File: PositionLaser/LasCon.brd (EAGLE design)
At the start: 44.4 x 28 mm, 10 parts

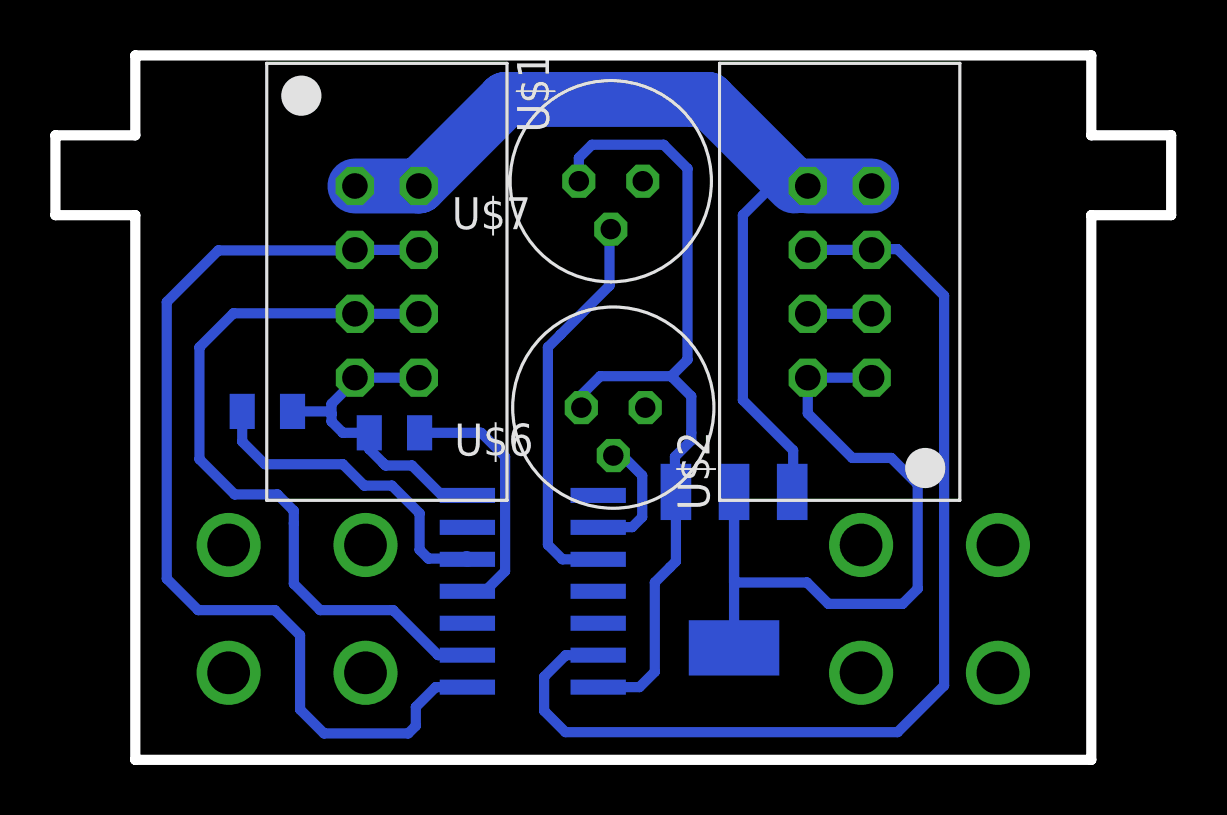
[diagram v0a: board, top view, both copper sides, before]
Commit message: Finished laser layout
Had to use one via. Will try and optimize it out later
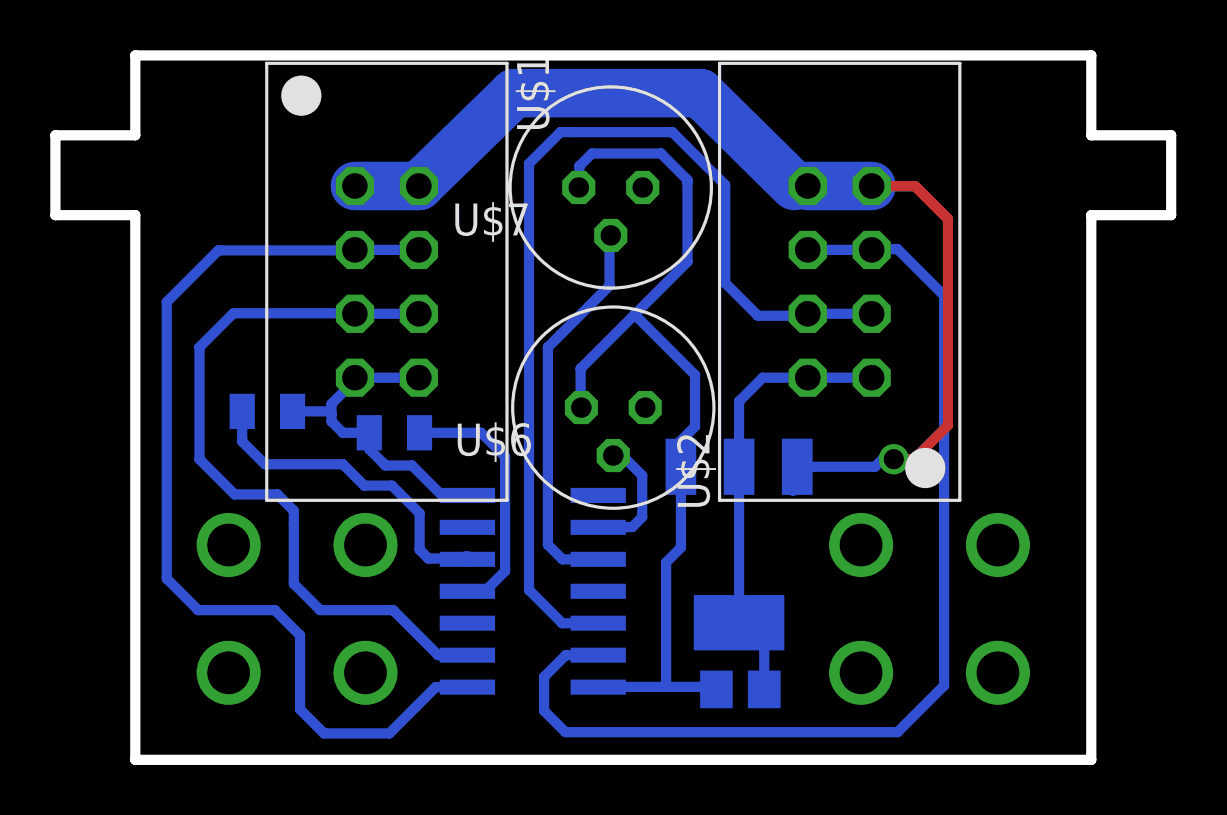
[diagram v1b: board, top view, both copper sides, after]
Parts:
- added U$10: (no value), GW-devices:C0805
- moved IC1 1.02 mm to (5.00, -10.4)
- moved U$7 0.25 mm to (-0.10, 3.75)
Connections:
- net +3V3: now also U$10.1
- net GND: now also U$10.2
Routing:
- net N$8: track 2.54 -> 39.7 mm
- net GND: track 44.6 -> 31.9 mm
- net N$1: track 38.0 -> 43.2 mm, vias 0 -> 1
- net +3V3: track 34.0 -> 37.6 mm
- added copper zone on layer 1, net GND
